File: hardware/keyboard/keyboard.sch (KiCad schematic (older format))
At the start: 3 parts, among them J1 Conn_01x06, U1 ProMicro

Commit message: update
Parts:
- J1: footprint (none) -> Connector_PinSocket_2.54mm:PinSocket_1x06_P2.54mm_Vertical
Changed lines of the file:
@@
 F 0 "J1" H 4600 2650 50  0000 C CNN
 F 1 "Conn_01x06" V 4473 2712 50  0001 R CNN
-F 2 "" H 4600 3100 50  0001 C CNN
+F 2 "Connector_PinSocket_2.54mm:PinSocket_1x06_P2.54mm_Vertical" H 4600 3100 50  0001 C CNN
 F 3 "~" H 4600 3100 50  0001 C CNN
 	1    4600 3100
@@
 	5500 3550 5950 3550
 $Comp
-L power:+5V #PWR?
+L power:+5V #PWR0101
 U 1 1 5FB4E853
 P 4900 2900
-F 0 "#PWR?" H 4900 2750 50  0001 C CNN
+F 0 "#PWR0101" H 4900 2750 50  0001 C CNN
 F 1 "+5V" V 4900 3100 50  0000 C CNN
 F 2 "" H 4900 2900 50  0001 C CNN
@@
 	4800 2800 4900 2800
 $Comp
-L power:GND #PWR?
+L power:GND #PWR0102
 U 1 1 5FB4E859
 P 4900 2800
-F 0 "#PWR?" H 4900 2550 50  0001 C CNN
+F 0 "#PWR0102" H 4900 2550 50  0001 C CNN
 F 1 "GND" V 4900 2600 50  0000 C CNN
 F 2 "" H 4900 2800 50  0001 C CNN

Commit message: Update ProMicro footprint
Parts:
- U1: footprint kbd:ProMicro_v3 -> arduino:ProMicro_v3
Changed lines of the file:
@@
 F 0 "U1" H 6650 5043 60  0000 C CNN
 F 1 "ProMicro" H 6650 4937 60  0000 C CNN
-F 2 "kbd:ProMicro_v3" H 6650 4831 60  0000 C CNN
+F 2 "arduino:ProMicro_v3" H 6650 4831 60  0000 C CNN
 F 3 "" H 6750 3050 60  0000 C CNN
 	1    6650 4100

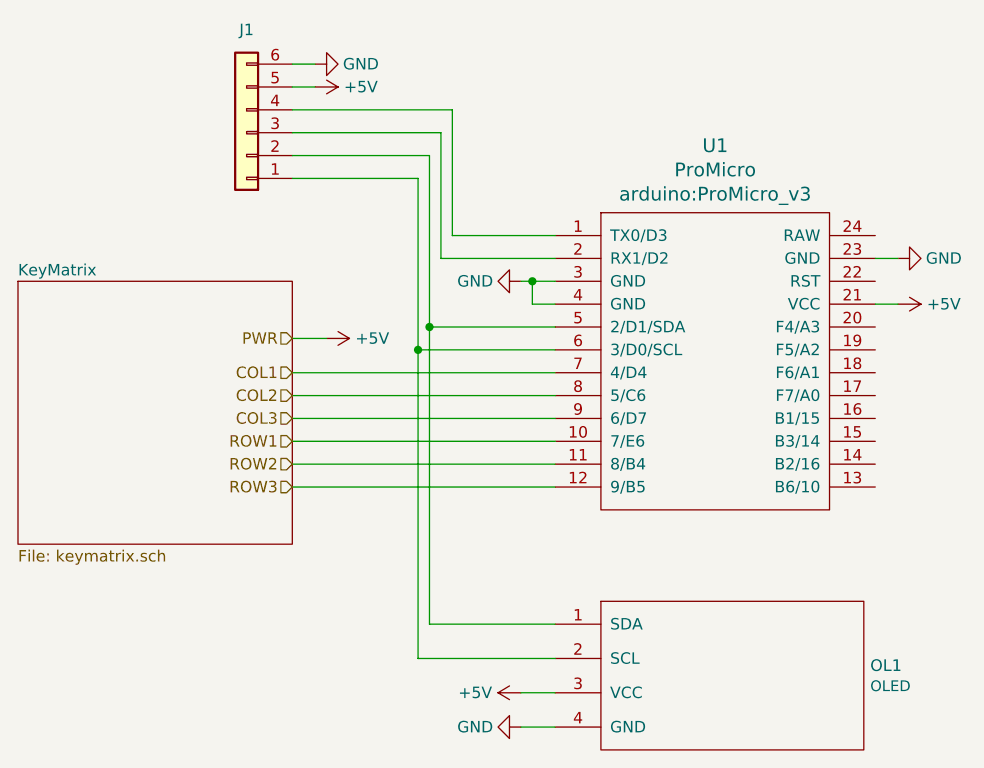
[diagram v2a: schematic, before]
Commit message: Fixed broken connections in hierarchy
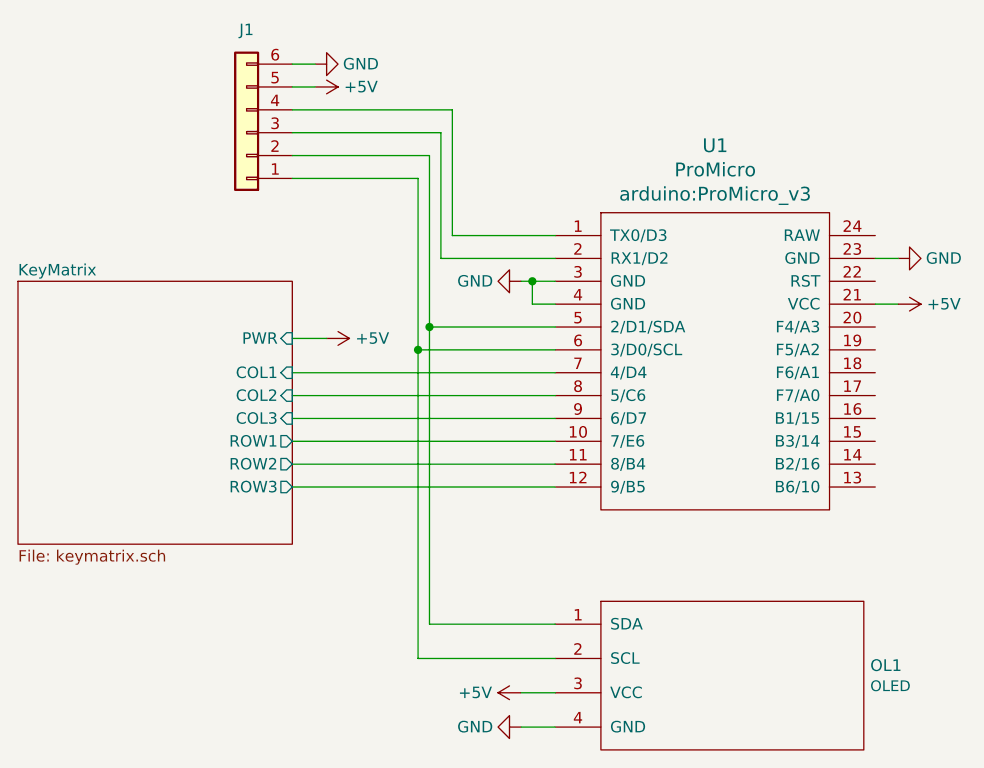
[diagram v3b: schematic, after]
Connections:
- net COL1 renamed KeyMatrix/COL1
- net COL2 renamed KeyMatrix/COL2
- net COL3 renamed KeyMatrix/COL3
- net ROW1 renamed KeyMatrix/ROW1
- net ROW2 renamed KeyMatrix/ROW2
- net ROW3 renamed KeyMatrix/ROW3
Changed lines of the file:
@@
 F0 "KeyMatrix" 50
 F1 "keymatrix.sch" 50
+F2 "COL1" I R 4800 4150 50
+F3 "COL2" I R 4800 4250 50
+F4 "COL3" I R 4800 4350 50
+F5 "ROW1" O R 4800 4450 50
+F6 "ROW2" O R 4800 4550 50
+F7 "ROW3" O R 4800 4650 50
+F8 "PWR" I R 4800 4000 50
 $EndSheet
-Text HLabel 4800 4150 0    50   Input ~ 0
-COL1
-Text HLabel 4800 4250 0    50   Input ~ 0
-COL2
-Text HLabel 4800 4350 0    50   Input ~ 0
-COL3
-Text HLabel 4800 4450 0    50   Input ~ 0
-ROW1
-Text HLabel 4800 4550 0    50   Input ~ 0
-ROW2
-Text HLabel 4800 4650 0    50   Input ~ 0
-ROW3
-Text HLabel 4800 4000 0    50   Input ~ 0
-PWR
 $Comp
 L kbd:ProMicro U1
@@
 $EndComp
 Wire Wire Line
-	4800 4150 5950 4150
-Wire Wire Line
 	5950 4250 4800 4250
 Wire Wire Line
@@
 	0    -1   -1   0
 $EndComp
+Wire Wire Line
+	4800 4150 5950 4150
 $EndSCHEMATC
